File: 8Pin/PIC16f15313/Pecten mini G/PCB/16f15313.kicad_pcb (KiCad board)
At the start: 2 copper layers, 40.1 x 42.2 mm, 17 parts, among them J1 JACK DC, J2 USB_B, J3 TERMINAL BLOCK, J4 POWER HEADERS, J5 Conn_02x04_Odd_Even, J6 Conn_02x04_Odd_Even, J7 ICSP, SW1 RESET, SW2 CONTROL, U1 PIC16F15313

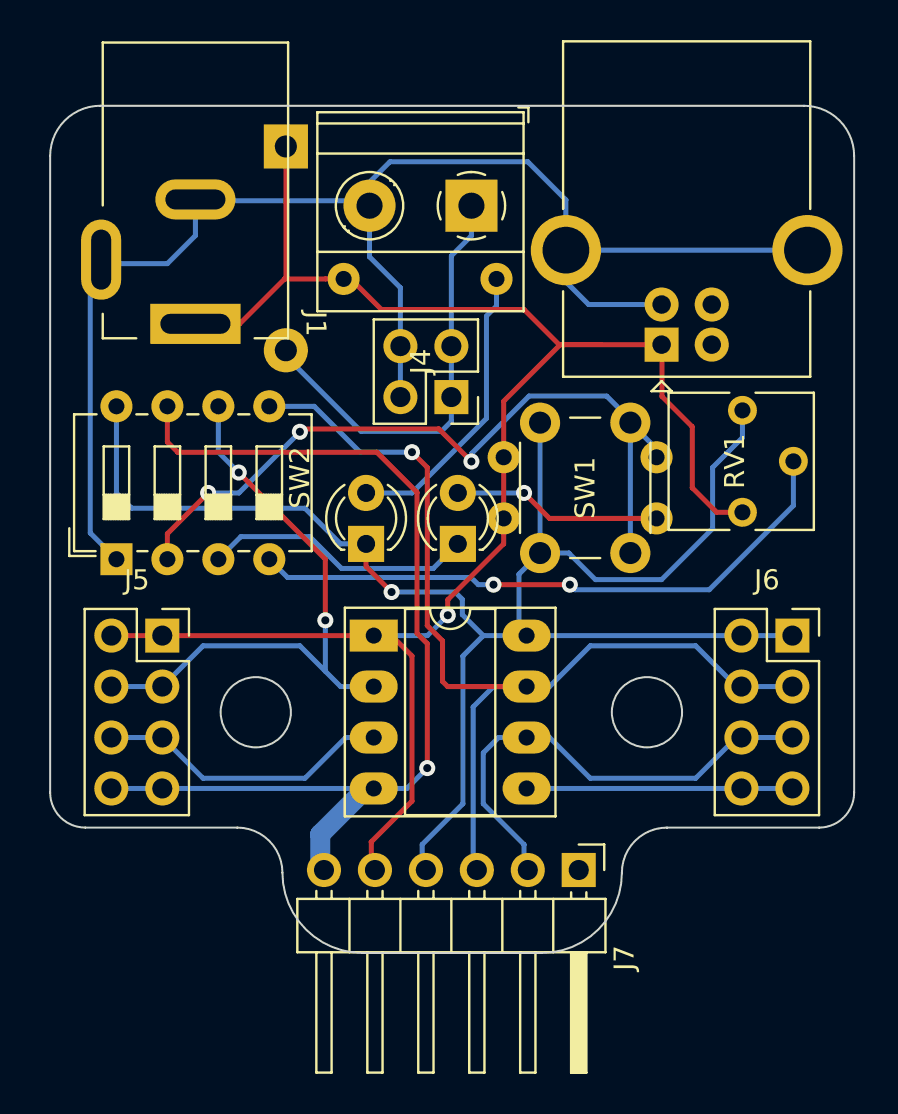
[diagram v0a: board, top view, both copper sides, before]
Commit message: Se finalizó el ruteo y forma de la PCB
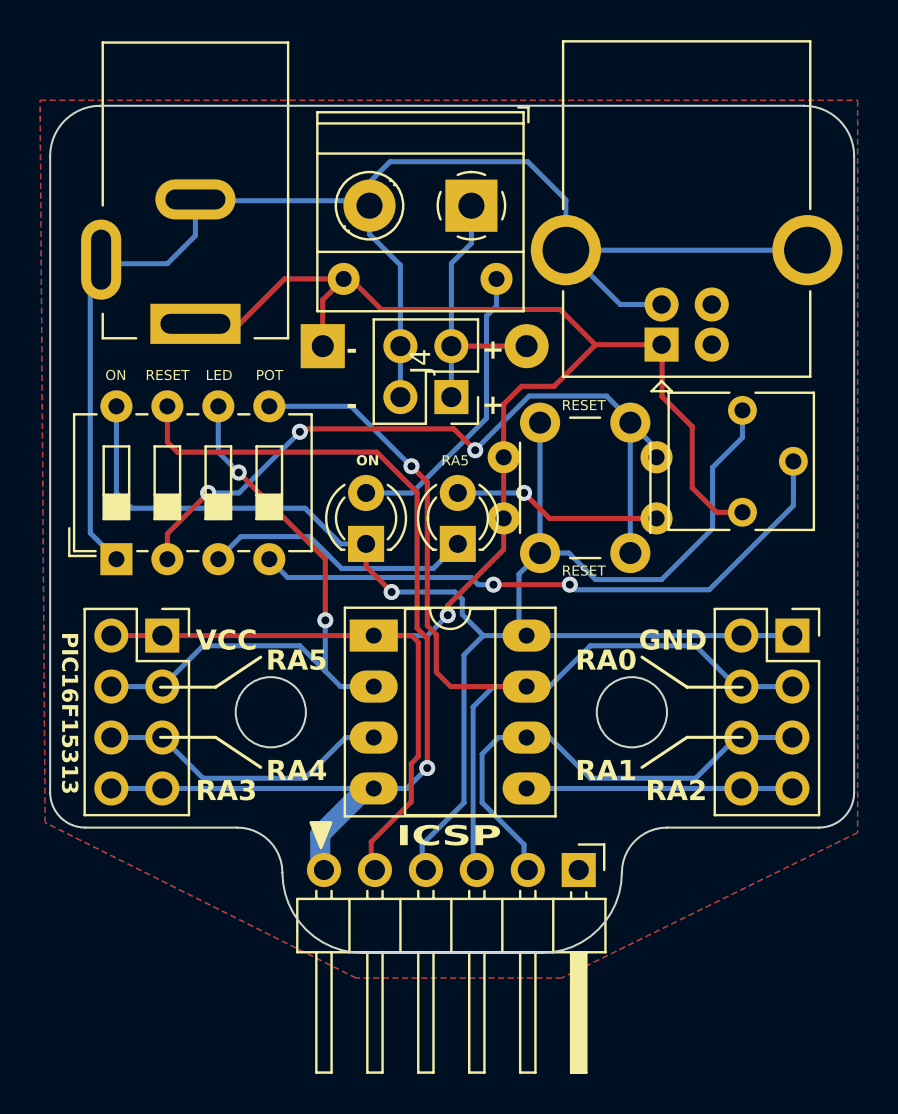
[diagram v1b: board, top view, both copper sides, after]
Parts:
- moved D1 10.1 mm to (124.8, 92.2), turned to 0 degrees
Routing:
- net Net-(D1-A): track 21.5 -> 13.7 mm
- net VCC: track 91.8 -> 89.7 mm
- net /on/off: track 76.0 -> 74.5 mm
- net /reset: track 38.2 -> 37.5 mm
- net /pgd: track 50.2 -> 49.7 mm
- added copper zone on B.Cu, net GND
- added copper zone on F.Cu, net VCC
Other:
- outline, holes or cut-outs redrawn
- board text added: "+"
- board text added: "+ -"
- board text added: "-"
- board text added: "1K"
- board text added: "3.3v - 5v"
- board text added: "330"
- board text added: "Diseño: Ing. Mucio Fausto Gómez Vieyra"
- board text added: "GND"
- board text added: "ICSP"
- board text added: "LED"
- board text added: "ON"
- board text added: "PIC16F15313"
- board text added: "POT"
- board text added: "RA0"
- board text added: "RA1"
- board text added: "RA2"
- board text added: "RA3"
- board text added: "RA4"
- board text added: "RA5"
- board text added: "RESET"
- board text added: "USB POWER ONLY NO DATA"
- board text added: "VCC"

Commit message: Se terminó la serigrafía de la tarjeta de desarrollo Pecten mini G
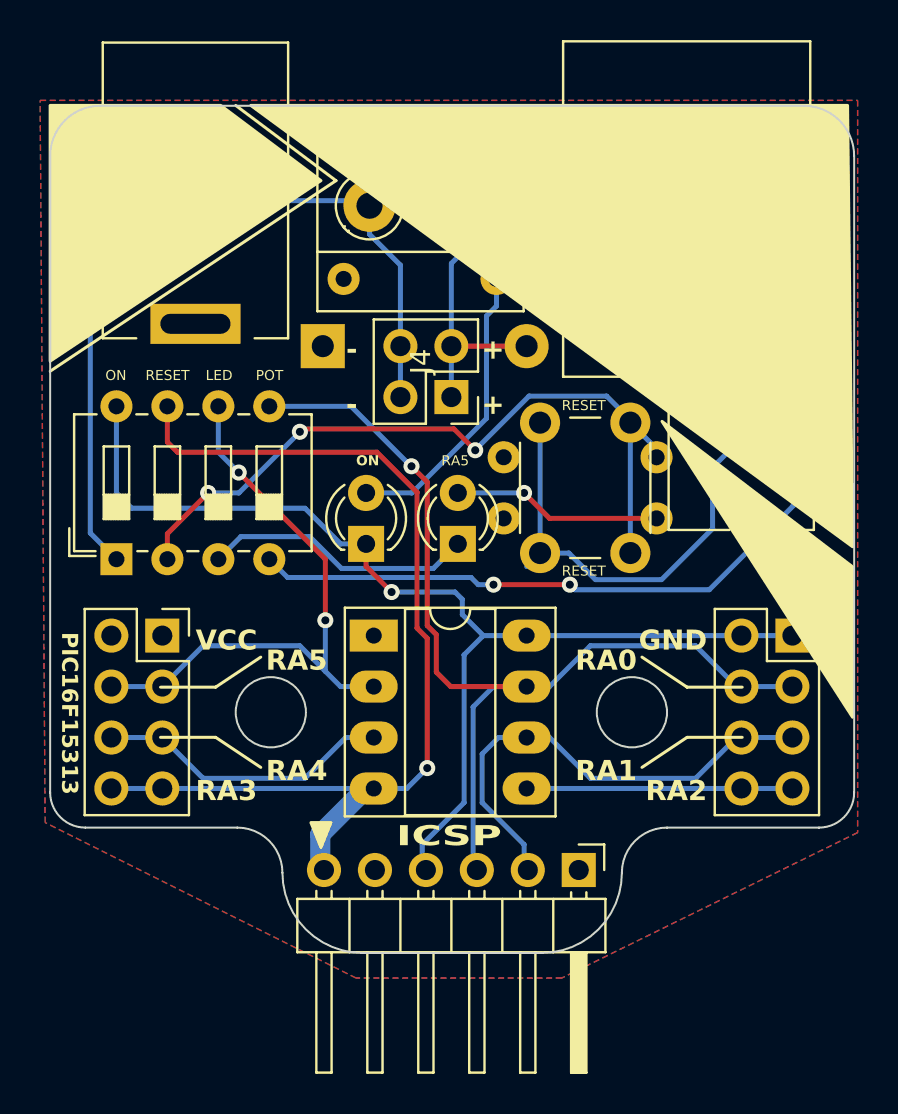
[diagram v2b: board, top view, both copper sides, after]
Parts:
- added G***: LOGO, LOGO, B.Cu at (118.8, 100.0)
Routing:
- net VCC: track 89.7 -> 0.00 mm, vias 1 -> 0
- net GND: track 82.8 -> 79.7 mm
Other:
- board text added: "mgv3d.com"
